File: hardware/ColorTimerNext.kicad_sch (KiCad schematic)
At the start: 0 parts

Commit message: KiCadで回路図作成
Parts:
- added BZ1: Buzzer, symbol Device:Buzzer
- added D1: BLUE, symbol Device:LED_Small_Filled
- added D2: RED, symbol Device:LED_Small_Filled
- added J1: CON_PIN, symbol Connector:Conn_01x06_Pin
- added Q1: 2SC1815, Package_TO_SOT_THT:TO-92_Inline, symbol Transistor_BJT:2SC1815
- added R1: 330, symbol Device:R_Small_US
- added R2: 47, symbol Device:R_Small_US
- added R3: 1k, symbol Device:R_Small_US
- added SW1: TRRIGER, symbol Switch:SW_Push
- added U1: AE-ESP32-WROOM-32E-MINI, symbol AE:AE-ESP32-WROOM-32E-MINI
- added U2: OLED I2C, symbol OLED:OLED-I2C
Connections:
- new net: SW1.2, U1. (IO15)
- new net: Q1.3 (B), R3.1
- new net: R3.2, U1. (IO15)
- new net: U1. (IO15), U2. (SDA) (x2)
- new net: D2.1 (K), R1.1
- new net: D1.1 (K), R2.1
- new net: D2.2 (A), U1. (IO15)
- new net: D1.2 (A), U1. (IO15)
- new net: BZ1.2 (-), Q1.2 (C)
- new net: J1.2 (Pin_2), U1. (IO15)
- new net: J1.3 (Pin_3), U1. (IO15)
- new net: J1.4 (Pin_4), U1. (IO15)
- new net: J1.5 (Pin_5), U1. (IO15)
- new net: J1.6 (Pin_6), U1. (IO15)
- new net +3.3V: BZ1.1 (+), U1. (IO15), U2. (SDA)
- new net GND: Q1.1 (E), R1.2, R2.2, SW1.1, U1. (IO15), U2. (SDA)
- no-connect marks 0 -> 23

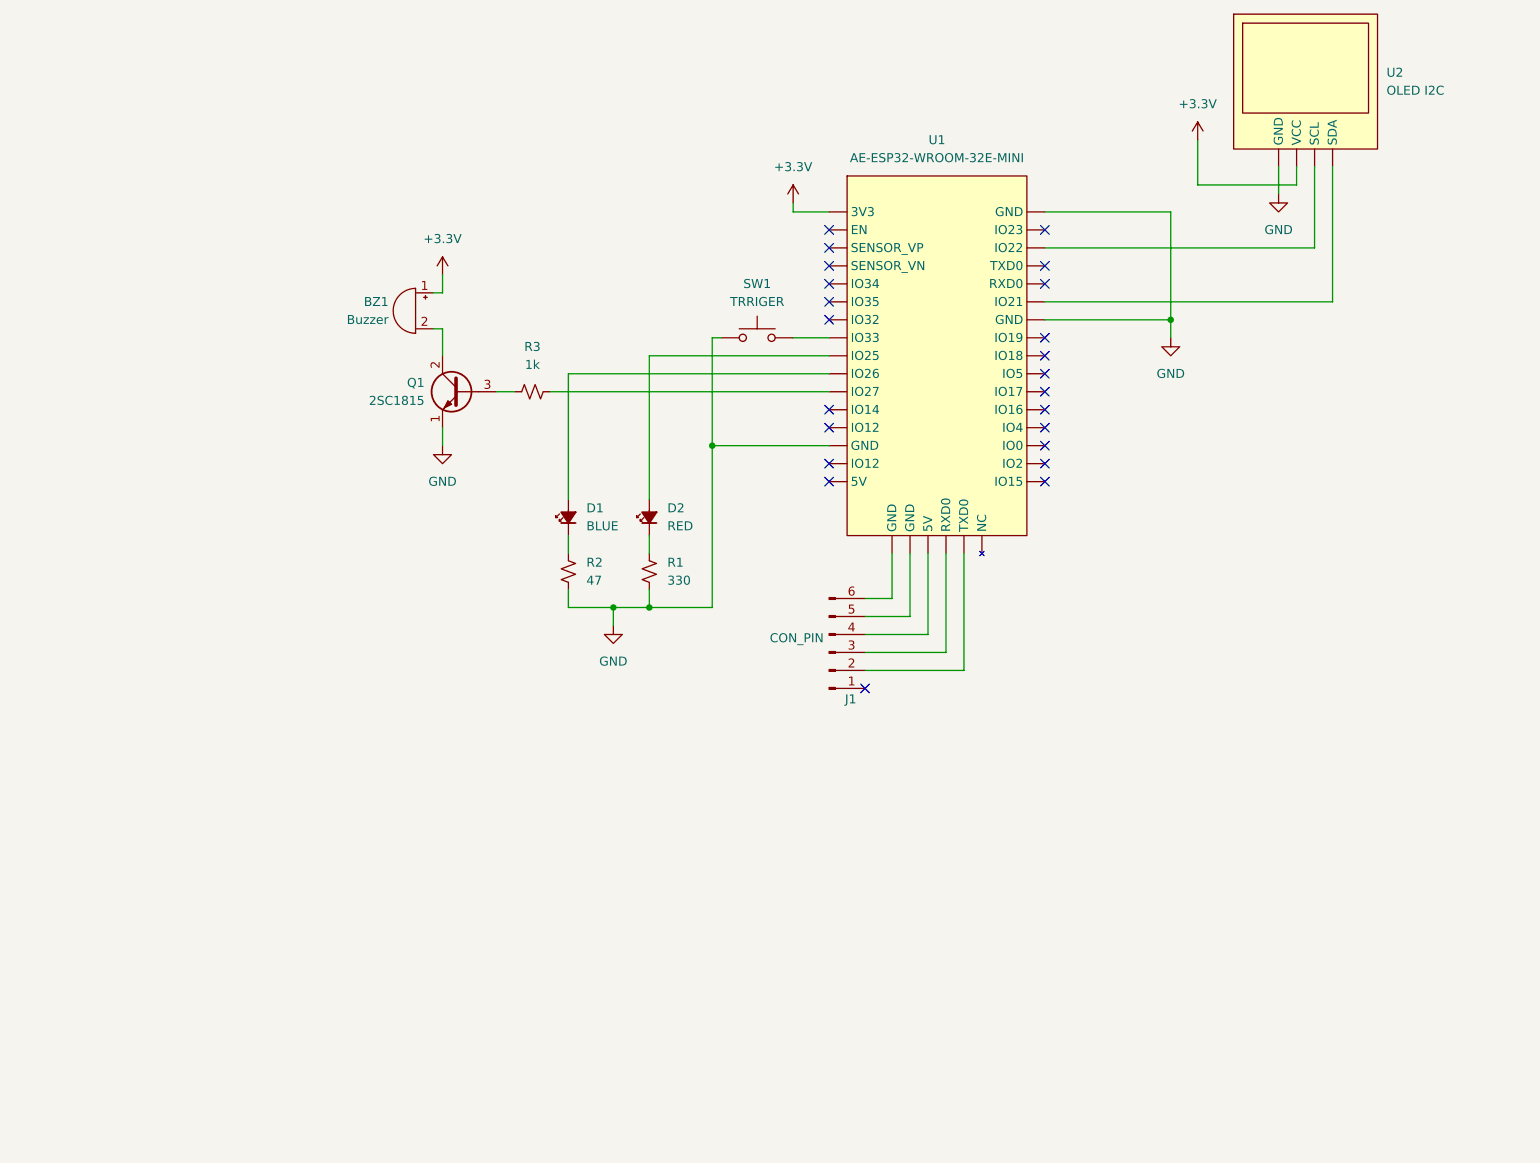
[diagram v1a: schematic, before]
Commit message: feat: add USB-UART hardware schematic
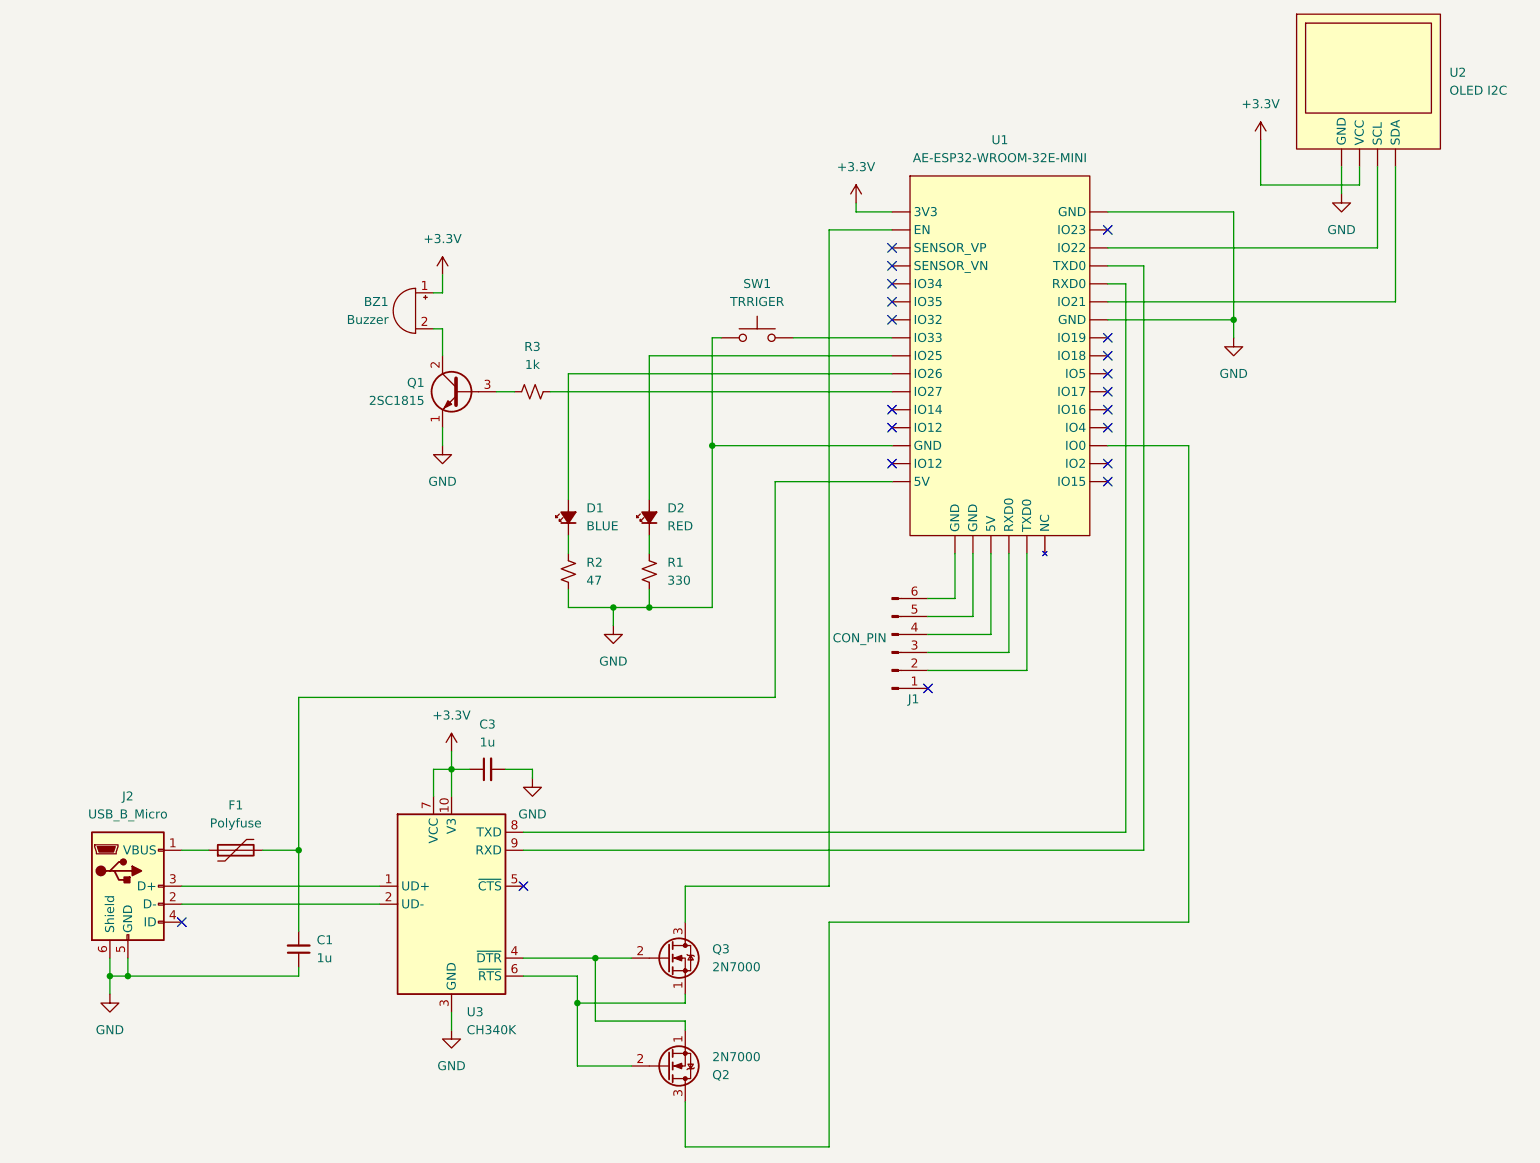
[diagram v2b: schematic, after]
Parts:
- added C1, C3: 1u, Capacitor_SMD:C_0603_1608Metric_Pad1.08x0.95mm_HandSolder, symbol Device:C_Small
- added F1: Polyfuse, Fuse:Fuse_1206_3216Metric_Pad1.42x1.75mm_HandSolder, symbol Device:Polyfuse
- added J2: USB_B_Micro, Connector_USB:USB_Micro-B_Molex-105017-0001, symbol Connector:USB_B_Micro
- added Q2, Q3: 2N7000, Package_TO_SOT_THT:TO-92_Inline, symbol Transistor_FET:2N7000
- added U3: CH340K, Package_SO:SSOP-10-1EP_3.9x4.9mm_P1mm_EP2.1x3.3mm, symbol Interface_USB:CH340K
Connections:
- net +3.3V: now also C3.1, U3.10 (V3), U3.7 (VCC)
- net GND: now also C1.1, C3.2, J2.5 (GND), J2.6 (Shield), U3.11 (GND), U3.3 (GND)
- new net: U1. (IO15), U2. (SDA) (x2)
- new net: J2.3 (D+), U3.1 (UD+)
- new net: J2.2 (D-), U3.2 (UD-)
- new net: Q2.1 (S), Q3.2 (G), U3.4 (~{DTR})
- new net: Q2.2 (G), Q3.1 (S), U3.6 (~{RTS})
- new net: U1. (IO15), U3.8 (TXD)
- new net: U1. (IO15), U3.9 (RXD)
- new net: F1.1, J2.1 (VBUS)
- new net: C1.2, F1.2, U1. (IO15)
- new net: Q3.3 (D), U1. (IO15)
- new net: Q2.3 (D), U1. (IO15)
- no-connect marks 23 -> 20
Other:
- moved on the sheet: J1, U1, U2

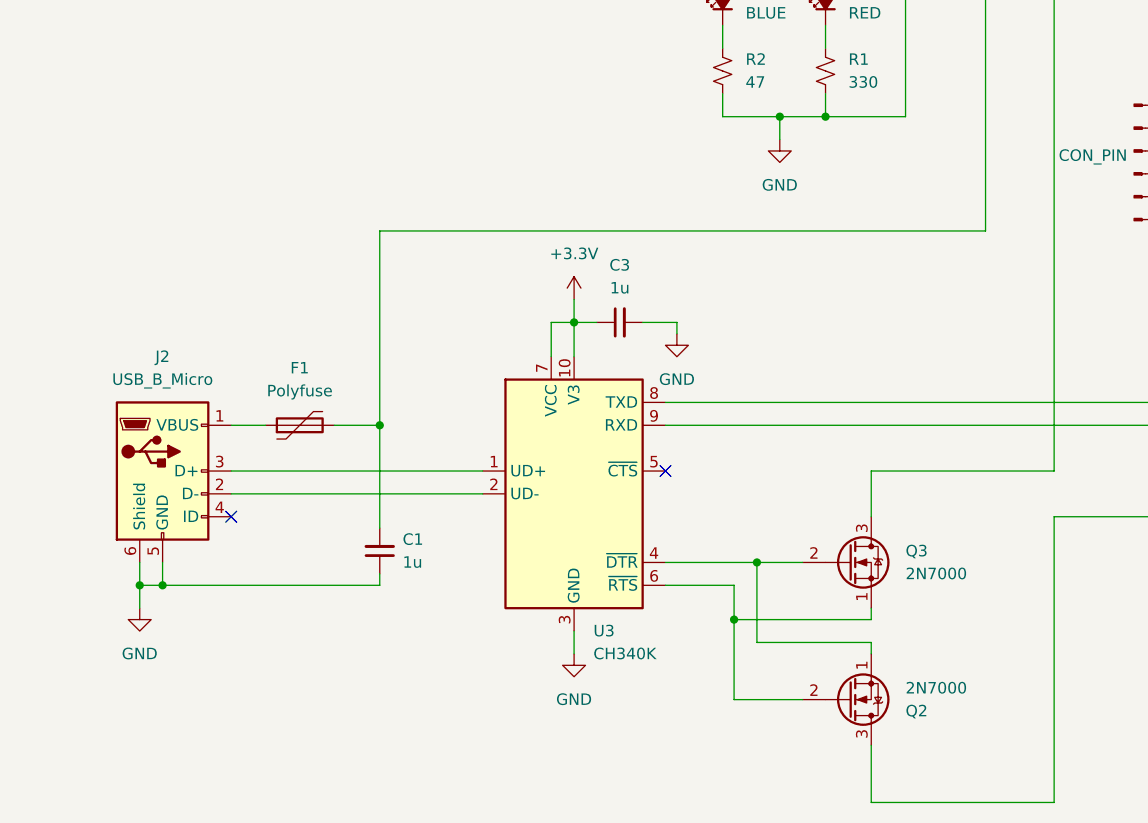
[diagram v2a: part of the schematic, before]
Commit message: feat: USB入力に逆流防止回路を追加する
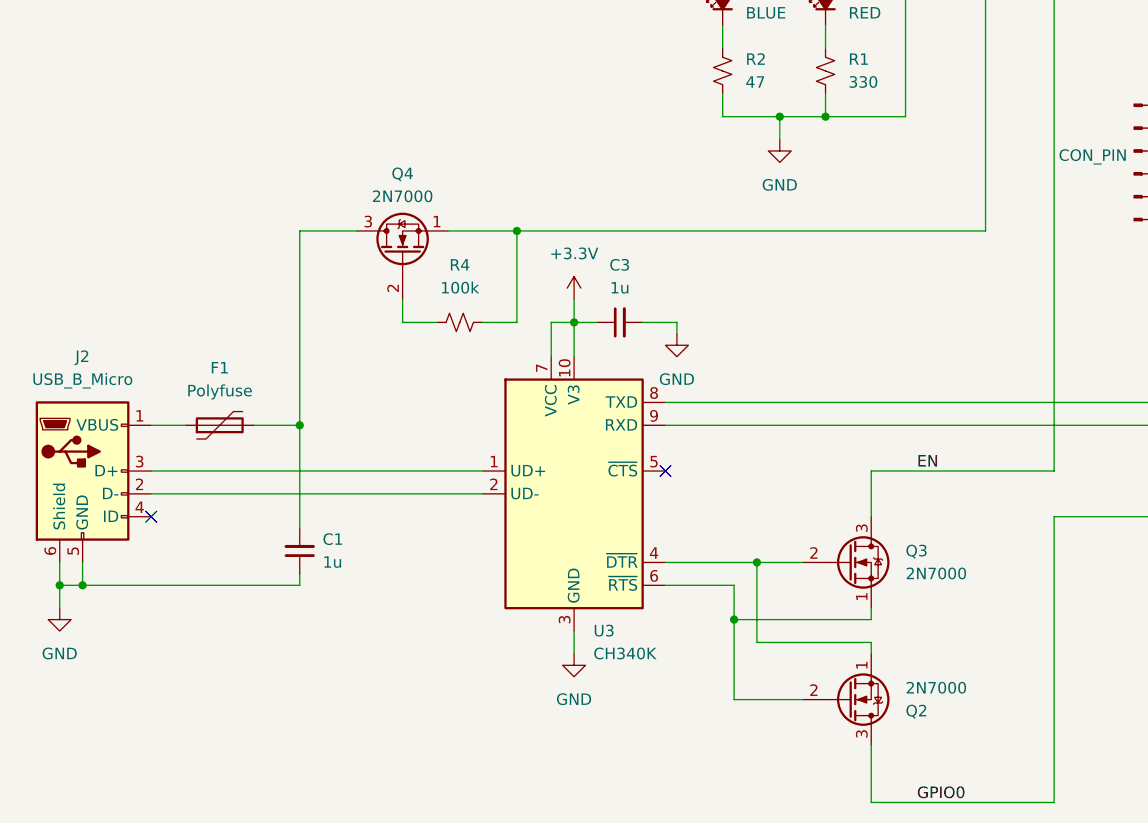
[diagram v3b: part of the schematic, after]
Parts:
- added Q4: 2N7000, Package_TO_SOT_THT:TO-92_Inline, symbol Transistor_FET:2N7000
- added R4: 100k, symbol Device:R_Small_US
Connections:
- net GPIO0: now reaches U1. (IO15)
- net GPIO0: now also Q2.3 (D); no longer U2. (SDA)
- net at C1.2, F1.2: now also Q4.3 (D); no longer U1. (IO15)
- net EN: now reaches Q3.3 (D), U1. (IO15)
- new net: U1. (IO15), U2. (SDA) (x2)
- new net: Q4.1 (S), R4.2, U1. (IO15)
- new net: Q4.2 (G), R4.1
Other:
- moved on the sheet: C1, F1, J2
